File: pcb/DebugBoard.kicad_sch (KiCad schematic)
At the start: 42 parts, among them J1 Debug, J2 12401598E4_2A, J3 Conn_01x04, J4 B8B-XH-A, Q1 S8050, SW5 B3U-1000P, U1 STM32H533VET6, U2 MCP2221A-I/ST, U3 AP2112K-3.3

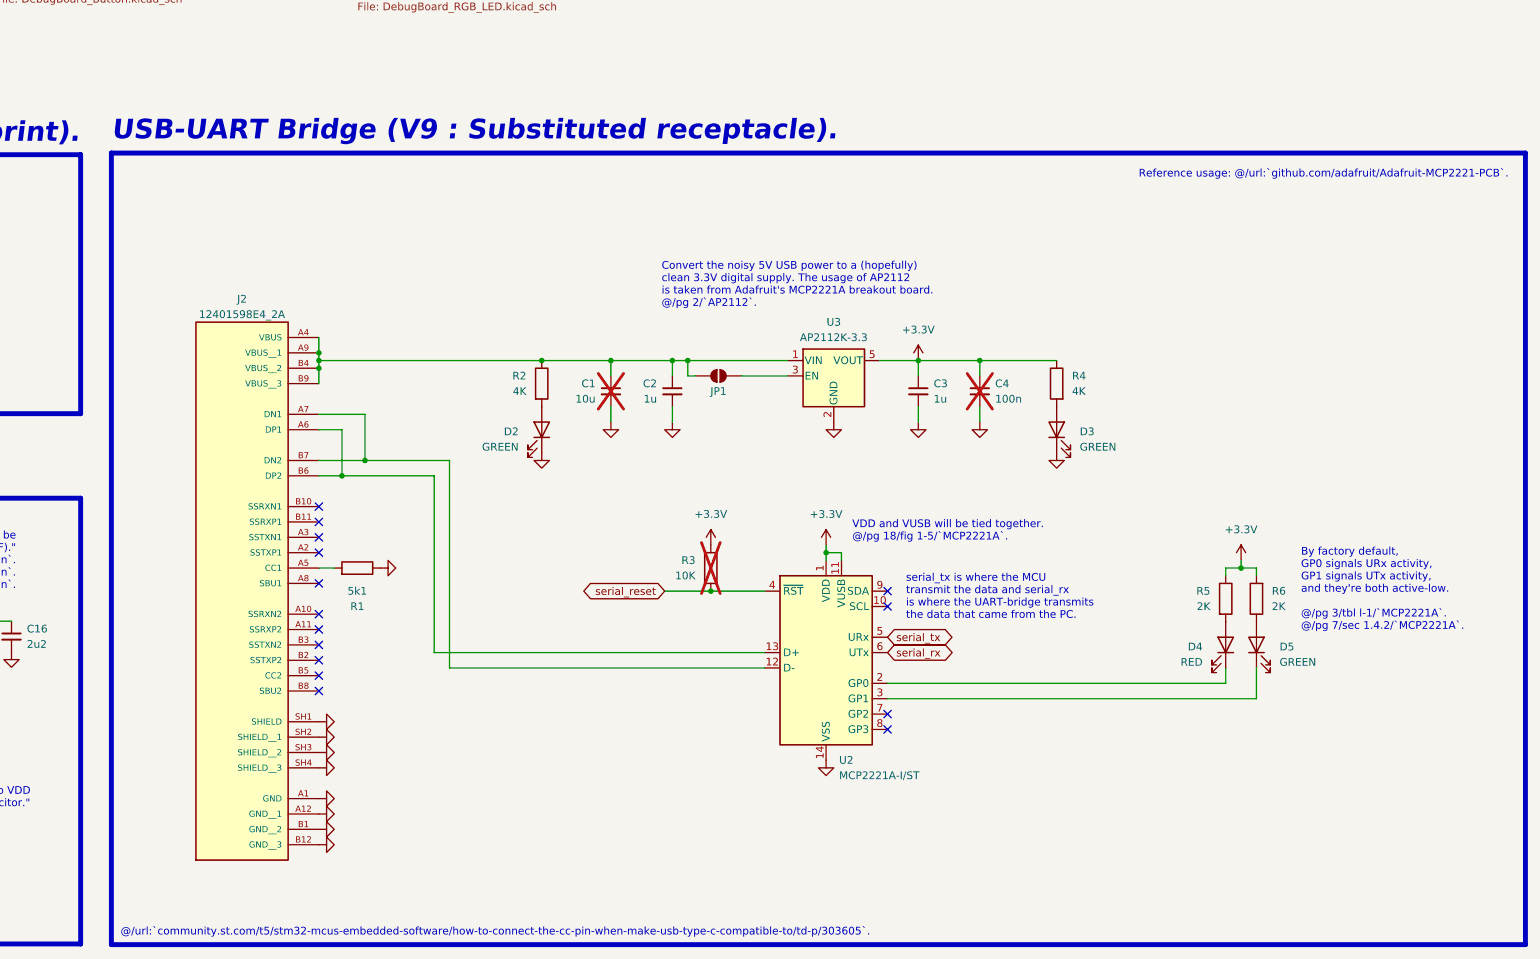
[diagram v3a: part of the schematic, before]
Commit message: Removed USB-UART bridge from `DebugBoard`.
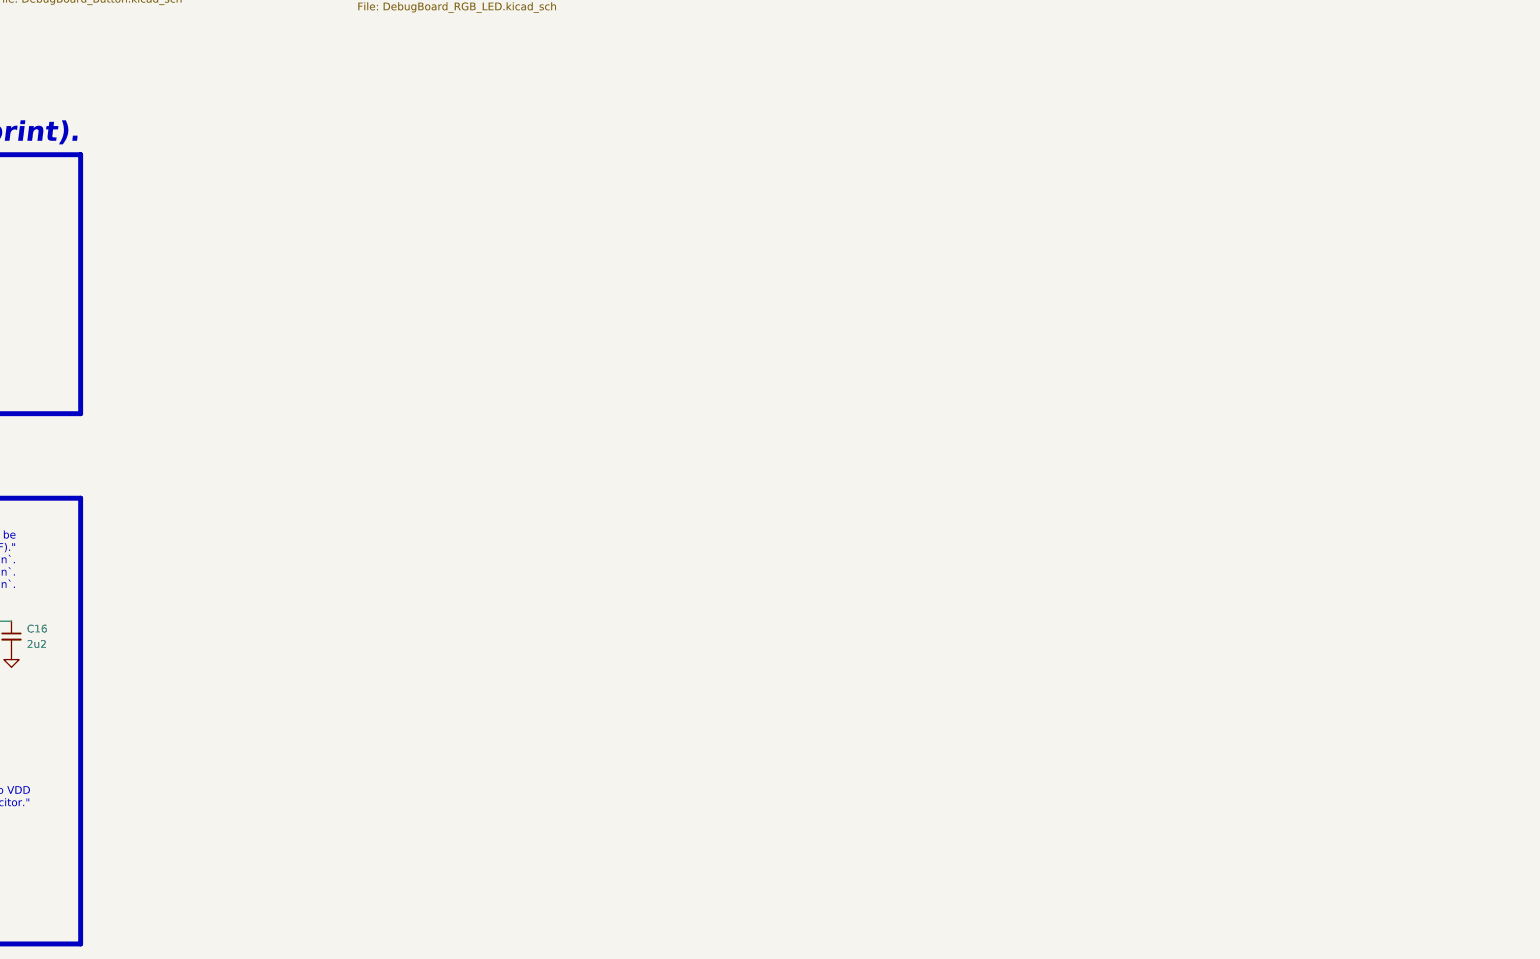
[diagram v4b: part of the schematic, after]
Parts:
- removed C1: 10u, Capacitor_SMD:C_1206_3216Metric_Pad1.33x1.80mm_HandSolder, symbol Device:C_Small
- removed C2, C3: 1u, Capacitor_SMD:C_1206_3216Metric_Pad1.33x1.80mm_HandSolder, symbol Device:C_Small
- removed C4: 100n, Capacitor_SMD:C_1206_3216Metric_Pad1.33x1.80mm_HandSolder, symbol Device:C_Small
- removed D2, D3, D5: GREEN, LED_SMD:LED_1206_3216Metric_Pad1.42x1.75mm_HandSolder, symbol Device:LED
- removed D4: RED, LED_SMD:LED_1206_3216Metric_Pad1.42x1.75mm_HandSolder, symbol Device:LED
- removed J2: 12401598E4_2A, pcb:AMPHENOL_12401598E4_2A, symbol 12401598E4_2A:12401598E4_2A
- removed JP1: SolderJumper_2_Open, Jumper:SolderJumper-2_P1.3mm_Open_RoundedPad1.0x1.5mm, symbol Jumper:SolderJumper_2_Open
- removed R1: 5k1, Resistor_SMD:R_1206_3216Metric_Pad1.30x1.75mm_HandSolder, symbol Device:R
- removed R2, R4: 4K, Resistor_SMD:R_1206_3216Metric_Pad1.30x1.75mm_HandSolder, symbol Device:R
- removed R3: 10K, Resistor_SMD:R_1206_3216Metric_Pad1.30x1.75mm_HandSolder, symbol Device:R
- removed R5, R6: 2K, Resistor_SMD:R_1206_3216Metric_Pad1.30x1.75mm_HandSolder, symbol Device:R
- removed U2: MCP2221A-I/ST, Package_SO:TSSOP-14_4.4x5mm_P0.65mm, symbol Interface_USB:MCP2221AxST
- removed U3: AP2112K-3.3, Package_TO_SOT_SMD:SOT-23-5, symbol Regulator_Linear:AP2112K-3.3
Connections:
- no-connect marks 64 -> 49
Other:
- note removed: "@/url:`community.st.com/t5/stm32-mcus-embedded-software/how-to-connect-the-cc-pin-when-make-usb-type-c-compatible-to/td-p/303605`."
- note removed: "By factory default, GP0 signals URx activity, GP1 signals UTx activity, and they're both active-low. @/pg 3/tbl l-1/`MCP2221A`. @/pg 7/sec 1.4.2/`MCP2221A`."
- note removed: "Convert the noisy 5V USB power to a (hopefully) clean 3.3V digital supply. The usage of AP2112 is taken from Adafruit's MCP2221A breakout board. @/pg 2/`AP2112`."
- note removed: "Reference usage: @/url:`github.com/adafruit/Adafruit-MCP2221-PCB`."
- note removed: "USB-UART Bridge (V9 : Substituted receptacle)."
- note removed: "VDD and VUSB will be tied together. @/pg 18/fig 1-5/`MCP2221A`."
- note removed: "serial_tx is where the MCU transmit the data and serial_rx is where the UART-bridge transmits the data that came from the PC."

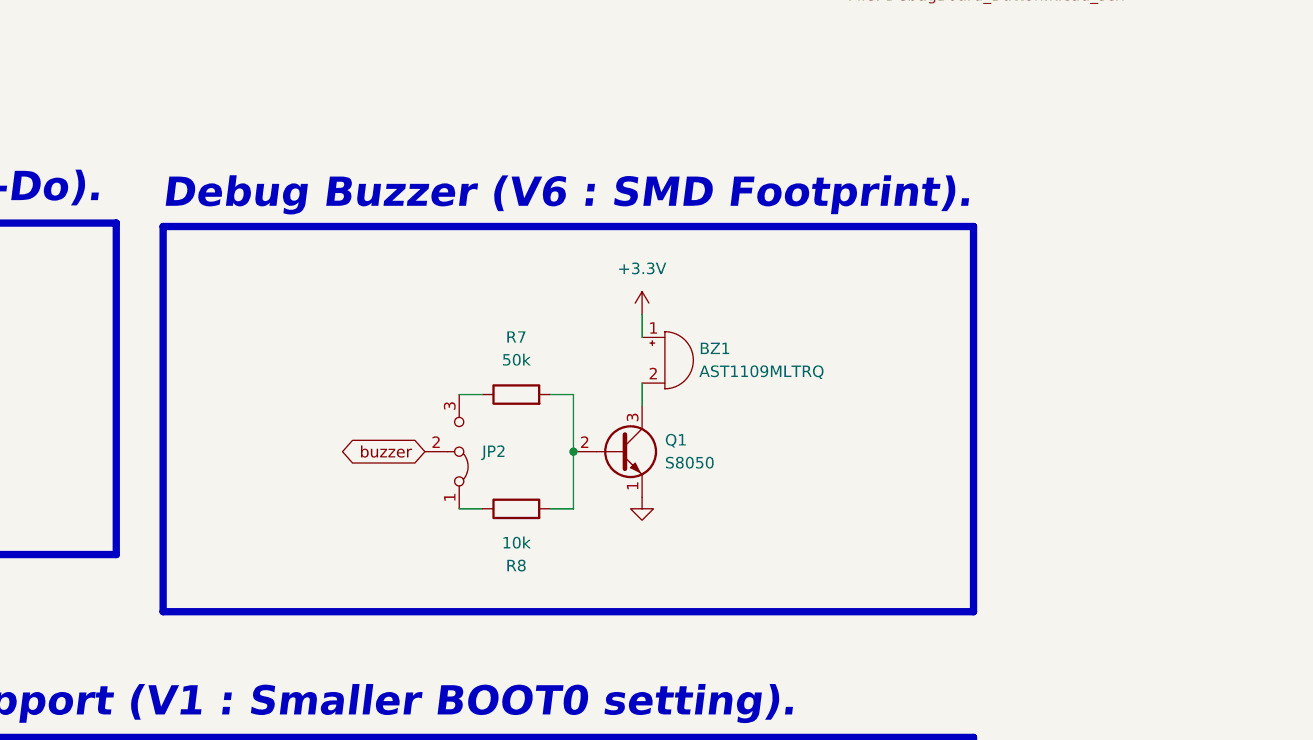
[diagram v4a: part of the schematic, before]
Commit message: Debug buzzer simplified.
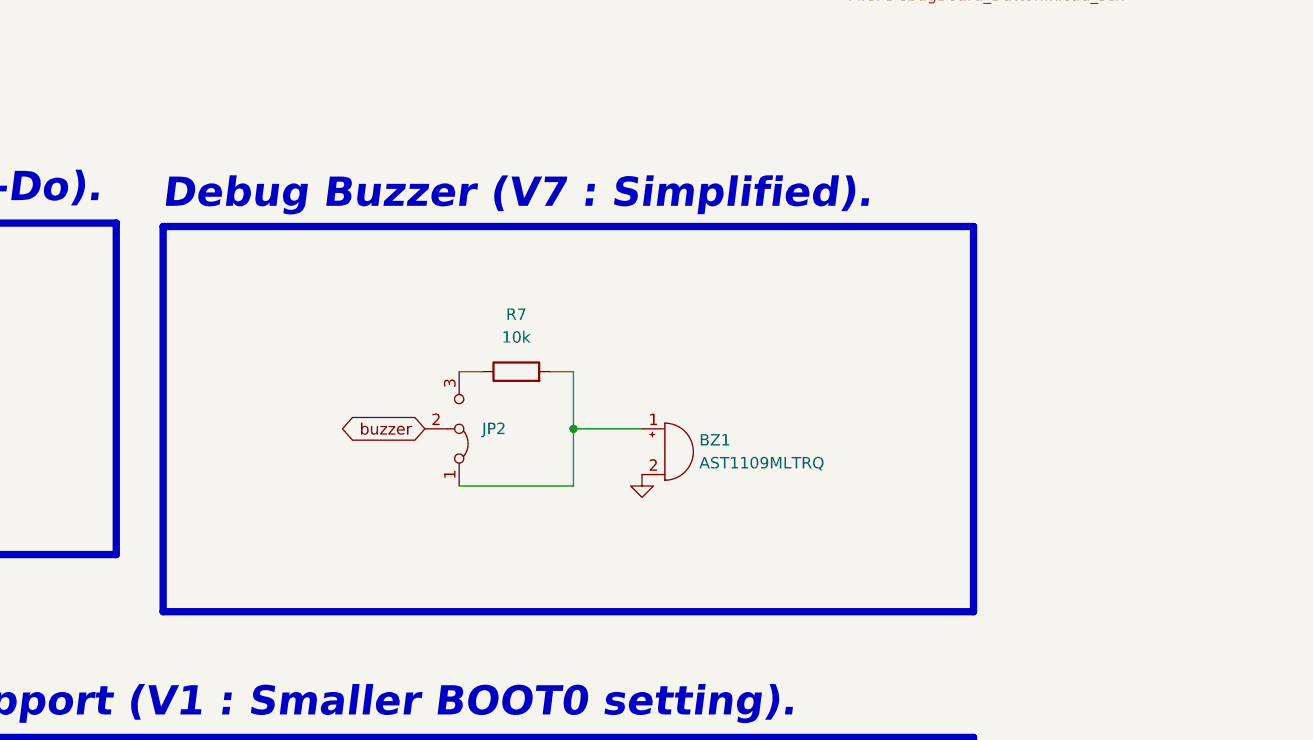
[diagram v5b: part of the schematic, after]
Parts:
- removed Q1: S8050, Package_TO_SOT_SMD:SOT-23_Handsoldering, symbol Transistor_BJT:S8050
- removed R8: 10k, Resistor_SMD:R_1206_3216Metric_Pad1.30x1.75mm_HandSolder, symbol Device:R
- R7: value 50k -> 10k
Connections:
- net +3.3V: no longer BZ1.1 (+)
- net GND: now also BZ1.2 (-)
- net at JP2.1 (A): now also BZ1.1 (+), R7.2
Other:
- note added: "Debug Buzzer (V7 : Simplified)."
- note removed: "Debug Buzzer (V6 : SMD Footprint)."
- moved on the sheet: BZ1, JP2, R7

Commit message: Made `DebugBoard` target and fixed some GPIO discrepancies.
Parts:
- added TP1, TP2: TestPoint, TestPoint:TestPoint_Bridge_Pitch2.0mm_Drill0.7mm, symbol Connector:TestPoint
- renumbered C8 to C1, C9 to C2, C10 to C3, C11 to C4, C12 to C5, C13 to C6, C14 to C7, C15 to C8, C16 to C9, J4 to J2, JP2 to JP1, R15 to R1, R7 to R2, SW5 to SW1
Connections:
- net button_A: no longer U1.42 (PE11)
- net button_B: no longer U1.43 (PE12)
- net display_i2c_clock: now also U1.47 (PB10); no longer U1.87 (PD6)
- net display_i2c_data: now also U1.51 (PB12); no longer U1.88 (PD7)
- net at U1.15 (PC0): now also TP1.1
- net at U1.16 (PC1): now also TP2.1
- net debug_i2c_clock renamed communication_i2c_clock
- net debug_i2c_data renamed communication_i2c_data
- net led_blue_A: no longer names the net of U1.70 (PA11)
- net led_blue_B: no longer names the net of U1.2 (PE3)
- net led_blue_C: no longer names the net of U1.5 (PE6)
- net led_blue_D: no longer names the net of U1.40 (PE9)
- net led_green_A: no longer names the net of U1.69 (PA10)
- net led_green_B: no longer names the net of U1.1 (PE2)
- net led_green_C: no longer names the net of U1.4 (PE5)
- net led_green_D: no longer names the net of U1.39 (PE8)
- net led_red_A: no longer names the net of U1.68 (PA9)
- net led_red_B: no longer names the net of U1.97 (PE0)
- net led_red_C: no longer names the net of U1.3 (PE4)
- net led_red_D: no longer names the net of U1.38 (PE7)
- net serial_reset: no longer names the net of U1.41 (PE10)
- net serial_rx: no longer names the net of U1.58 (PD11)
- net serial_tx: no longer names the net of U1.59 (PD12)
- no-connect marks 49 -> 64

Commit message: Laid out and routed `DebugBoard`.
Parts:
- added C13: 100n, Capacitor_SMD:C_1206_3216Metric_Pad1.33x1.80mm_HandSolder, symbol Device:C_Small
- added D5: GREEN, LED_SMD:LED_1206_3216Metric_Pad1.42x1.75mm_HandSolder, symbol Device:LED
- added JP2, JP3: Jumper_2_Small_Bridged, TestPoint:TestPoint_2Pads_Pitch2.54mm_Drill0.8mm, symbol Jumper:Jumper_2_Small_Bridged
- added R19: 100, Resistor_SMD:R_1206_3216Metric_Pad1.30x1.75mm_HandSolder, symbol Device:R
- added R20: 1K, Resistor_SMD:R_1206_3216Metric_Pad1.30x1.75mm_HandSolder, symbol Device:R
- added R21, R22, R23, R24, R25: 10k, Resistor_SMD:R_1206_3216Metric_Pad1.30x1.75mm_HandSolder, symbol Device:R
- added SW4: B3U-1000P, Button_Switch_SMD:SW_SPST_B3U-1000P, symbol Switch:SW_Push
- added TP3, TP4, TP5, TP6: TestPoint, TestPoint:TestPoint_Bridge_Pitch2.0mm_Drill0.7mm, symbol Connector:TestPoint
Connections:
- net +3.3V: now also JP2.1 (A), R19.1, R21.2, R22.2, R23.2, R24.2, R25.2, TP3.1; no longer J3.2 (Pin_2)
- net GND: now also C13.2, D5.1 (K), JP3.1 (A), R20.2, TP4.1, TP5.1, TP6.1; no longer J3.1 (Pin_1)
- net RESET: now also C13.1, R19.2, SW4.1
- net button_A: now also U1.45 (PE14)
- net button_B: now also U1.43 (PE12)
- net communication_i2c_clock: now also R22.1
- net communication_i2c_data: now also J2.6 (Pin_6), R21.1; no longer J2.4 (Pin_4)
- net led_channel_blue_A: now also U1.4 (PE5)
- net led_channel_blue_B: now also U1.87 (PD6)
- net led_channel_blue_C: now also U1.34 (PC5)
- net led_channel_blue_D: now also U1.70 (PA11)
- net led_channel_green_A: now also U1.3 (PE4)
- net led_channel_green_B: now also U1.85 (PD4)
- net led_channel_green_C: now also U1.32 (PA7)
- net led_channel_green_D: now also U1.69 (PA10)
- net led_channel_red_A: now also U1.2 (PE3)
- net led_channel_red_B: now also U1.86 (PD5)
- net led_channel_red_C: now also U1.33 (PC4)
- net led_channel_red_D: now also U1.68 (PA9)
- net communication_uart_rx_A: now reaches J2.3 (Pin_3)
- net communication_uart_rx_A: now also U1.54 (PB15), R24.1
- net at U1.15 (PC0): no longer TP1.1
- net at U1.16 (PC1): no longer TP2.1
- net communication_uart_rx_B: now reaches U1.36 (PB1)
- net communication_uart_rx_B: now also J2.4 (Pin_4), R23.1
- net testpoint_A: now reaches U1.41 (PE10)
- net testpoint_A: now also TP1.1
- net testpoint_B: now reaches U1.84 (PD3)
- net testpoint_B: now also TP2.1
- new net: D5.2 (A), R25.1
- new net: R20.1, SW4.2
- new net: J3.1 (Pin_1), JP2.2 (B)
- new net: J3.2 (Pin_2), JP3.2 (B)
- no-connect marks 64 -> 46
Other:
- note added: "Pin order can seem to vary depending on what module is used."
- note added: "Reset Mechanism (V4 : Removed local-net)."
- moved on the sheet: TP1, TP2

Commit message: Placed silkscreen for `DebugBoard`.
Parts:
- renumbered C6 to C1, C13 to C10, C9 to C2, C2 to C6, C1 to C7, C7 to C9, D5 to D4, H3 to H1, H1 to H3, J3 to J2, J2 to J3, JP2 to JP1, JP3 to JP2, JP1 to JP3, R2 to R10, R21 to R11, R22 to R12, R23 to R13, R24 to R14, R1 to R2, R25 to R21, R19 to R3, R20 to R7, SW4 to SW1, SW1 to SW2, TP2 to TP1, TP4 to TP2, TP6 to TP3, TP5 to TP4, TP1 to TP5, TP3 to TP6
